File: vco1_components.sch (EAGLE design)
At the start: 56 parts, among them IC1 LM13700N, Q3 2N3904, Q4 2N3904, U1 TL072_, U2 TL072_, U3 TL072_

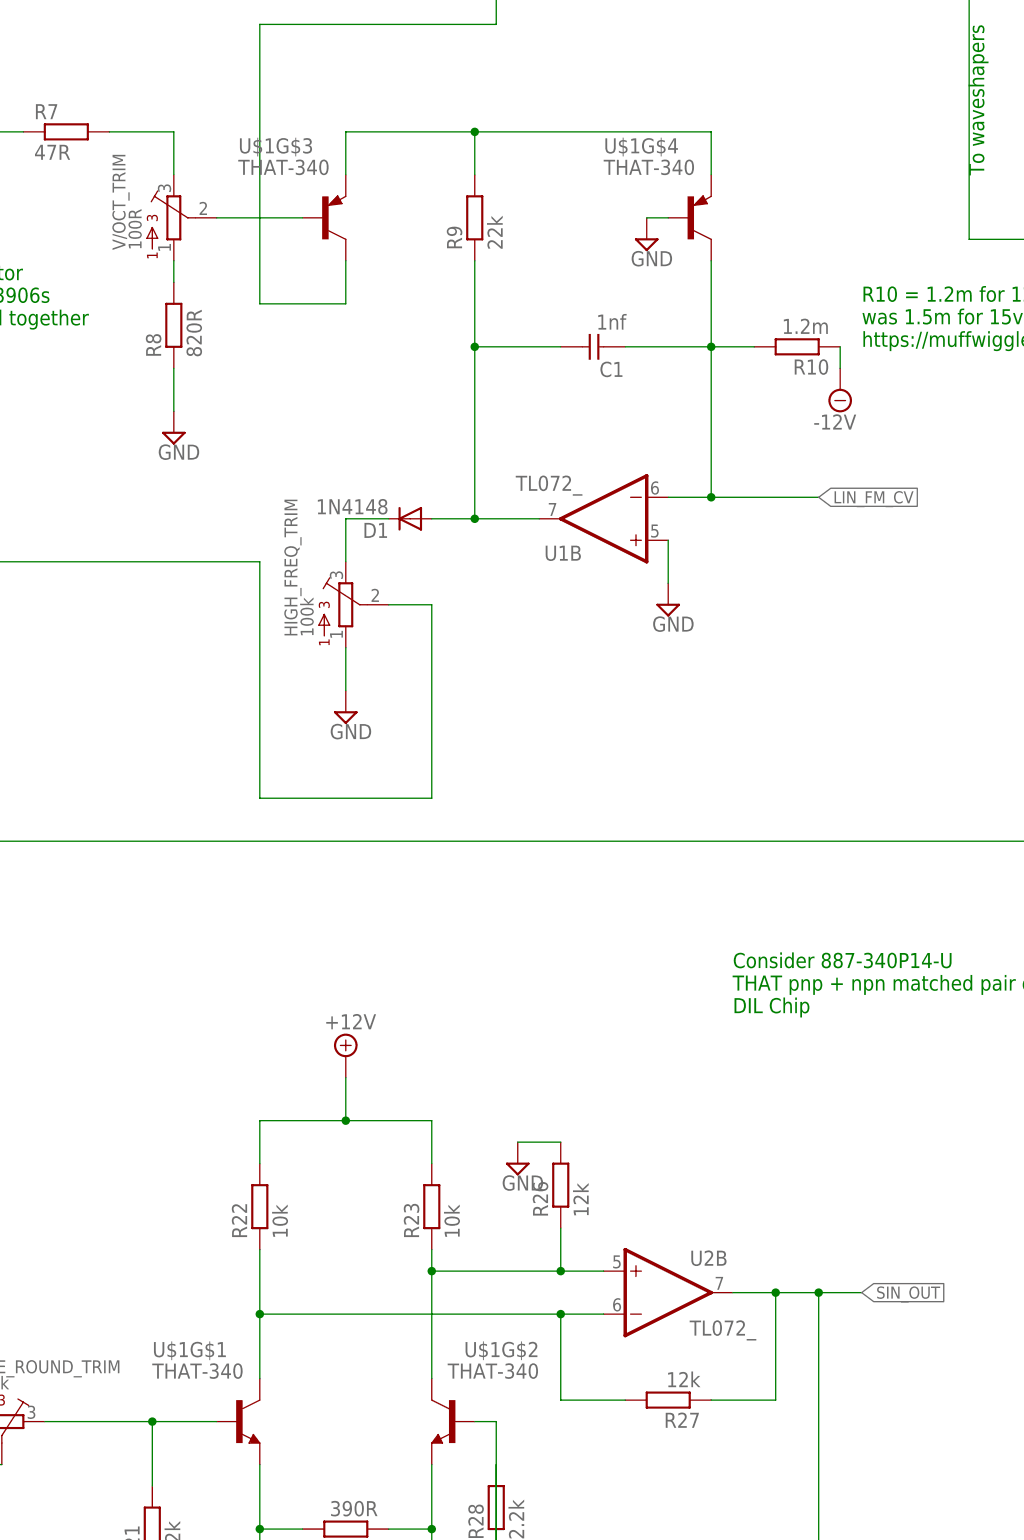
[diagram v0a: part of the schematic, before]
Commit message: Transistor outlines on THAT 340
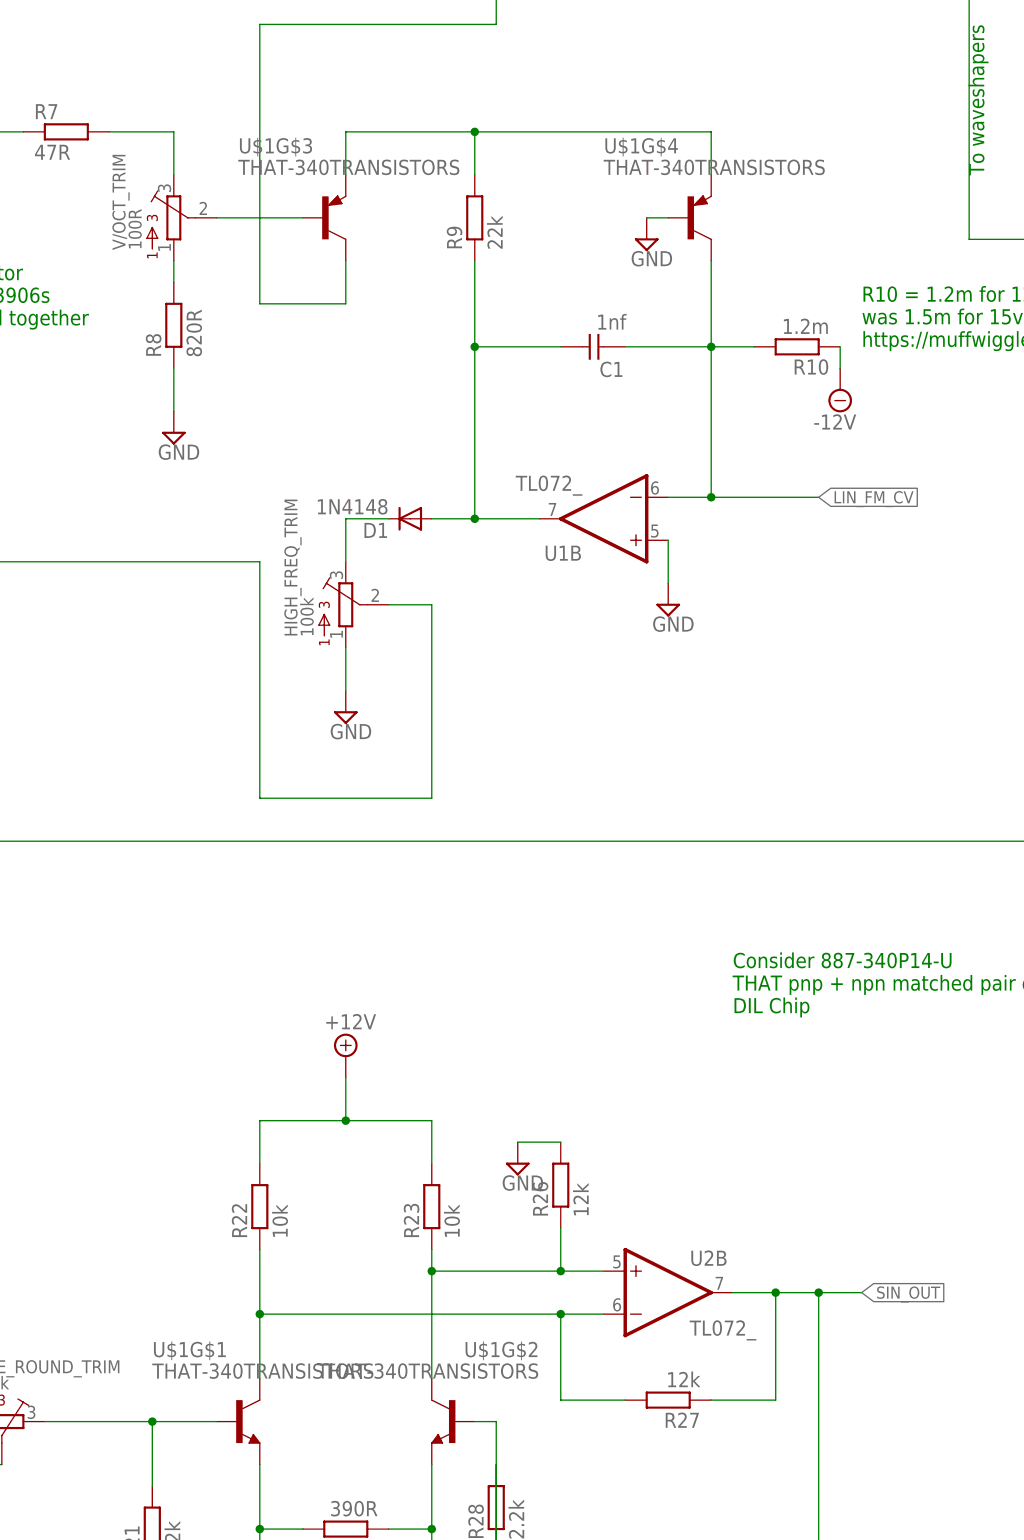
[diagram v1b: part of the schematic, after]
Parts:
- U$1: value THAT-340 -> THAT-340TRANSISTORS; device MusicThingModular:THAT-340 -> MusicThingModular:THAT-340TRANSISTORS
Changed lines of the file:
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@@
 <?xml version="1.0" encoding="utf-8"?>
 <!DOCTYPE eagle SYSTEM "eagle.dtd">
-<eagle version="7.4.0">
+<eagle version="7.2.0">
 <drawing>
 <settings>
@@
 <part name="SUPPLY38" library="supply2" deviceset="GND" device=""/>
 <part name="R36" library="MusicThingModular" deviceset="RESISTOR" device="7MM" value="150k"/>
-<part name="U$1" library="MusicThingModular" deviceset="THAT-340" device=""/>
+<part name="U$1" library="MusicThingModular" deviceset="THAT-340" device="TRANSISTORS"/>
 <part name="SV1" library="MusicThingModular" deviceset="EURO_POWER_HEADER" device="LOCK_PADS"/>
 <part name="SUPPLY39" library="supply2" deviceset="-12V" device=""/>
